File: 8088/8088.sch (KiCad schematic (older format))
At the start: 91 parts, among them CON1 BARREL_JACK, P1 CONN_02X20, P2 CONN_01X02, SW1 STEP_CLK, SW2 RESET, SW3 PWR, U1 8284, U10 2114, U11 ULN2803ADWR, U12 74LS14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

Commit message: Fixed schematic errors and added custom component footprints for the switches/PBs
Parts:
- added D31: AD0, LEDs:LED_1206_HandSoldering, symbol Led_Small
- added D32: AD1, LEDs:LED_1206_HandSoldering, symbol Led_Small
- added D33: AD2, LEDs:LED_1206_HandSoldering, symbol Led_Small
- added D34: AD3, LEDs:LED_1206_HandSoldering, symbol Led_Small
- added D35: PWR, LEDs:LED_1206_HandSoldering, symbol Led_Small
- added R33, R34, R35, R36: 1K, Resistors_SMD:R_0805_HandSoldering, symbol R_Small
- added R37: 220, Resistors_SMD:R_0805_HandSoldering, symbol R_Small
- added unit 2 of U12
- added unit 3 of U12
- added unit 4 of U12
- added unit 5 of U12
- D27: value AD0 -> DEN
- D28: value AD2 -> IO/~M
- D29: value AD3 -> RD
- D30: value AD4 -> WR
- JP1: value PROG/READ -> CLK_SEL
- SW1, SW2: footprint (none) -> Library:PB2PIN
- SW3: footprint (none) -> Library:SPST-SLIDE
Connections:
- net labels added: IO/~M, ~DEN, ~RD, ~WR
- net labels removed: VDD
- wire segments 557 -> 536
- no-connect marks 26 -> 18
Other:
- moved on the sheet: D27, D28, D29, D30, R29, R30, R31, R32

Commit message: Started PCB
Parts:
- removed U16: LM7805, TO_SOT_Packages_SMD:TO-252-3_TabPin2, symbol LM7805
- added U16: 7805, TO_SOT_Packages_SMD:TO-252-3_TabPin2, symbol 7805
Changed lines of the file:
@@
-$EndComp
-$Comp
-L LM7805 U16
-U 1 1 59D01B37
-P 19300 7650
-F 0 "U16" H 19450 7454 50  0000 C CNN
-F 1 "LM7805" H 19300 7850 50  0000 C CNN
-F 2 "TO_SOT_Packages_SMD:TO-252-3_TabPin2" H 19300 7650 50  0001 C CNN
-F 3 "" H 19300 7650 50  0000 C CNN
-	1    19300 7650
-	1    0    0    -1
 $EndComp
 $Comp
@@
 	20550 8000 20550 7900
 Connection ~ 19900 8000
+$Comp
+L 7805 U16
+U 1 1 59C7D17F
+P 19300 7650
+F 0 "U16" H 19450 7454 50  0000 C CNN
+F 1 "7805" H 19300 7850 50  0000 C CNN
+F 2 "TO_SOT_Packages_SMD:TO-252-3_TabPin2" H 19300 7650 50  0001 C CNN
+F 3 "" H 19300 7650 50  0000 C CNN
+	1    19300 7650
+	1    0    0    -1
+$EndComp
 $EndSCHEMATC

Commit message: Initial PCB design finished
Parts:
- removed P1: CONN_02X20, Pin_Headers:Pin_Header_Straight_2x20_Pitch2.54mm, symbol CONN_02X20
- added P1: U3PA, Pin_Headers:Pin_Header_Straight_1x08_Pitch2.54mm, symbol CONN_01X08
- added P3: U3PB, Pin_Headers:Pin_Header_Straight_1x08_Pitch2.54mm, symbol CONN_01X08
- added P4: RX/TX, Pin_Headers:Pin_Header_Straight_1x02_Pitch2.54mm, symbol CONN_01X02
- added P5: U4PC, Pin_Headers:Pin_Header_Straight_1x06_Pitch2.54mm, symbol CONN_01X06
- added P6: U4PA, Pin_Headers:Pin_Header_Straight_1x08_Pitch2.54mm, symbol CONN_01X08
- added P7: U4PB, Pin_Headers:Pin_Header_Straight_1x08_Pitch2.54mm, symbol CONN_01X08
- added P8: GND, Pin_Headers:Pin_Header_Straight_2x02_Pitch2.54mm, symbol CONN_01X04
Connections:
- wire segments 536 -> 535
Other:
- moved on the sheet: P2

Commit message: Fixed schematic error
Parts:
- U10, U9: symbol 2114 -> 2114-RESCUE-8088
- U16: symbol 7805 -> 7805-RESCUE-8088
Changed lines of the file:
@@
 EESchema Schematic File Version 2
+LIBS:8088-rescue
 LIBS:8088
-LIBS:ab2_7segment
-LIBS:ab2_audio
-LIBS:ab2_buffer
-LIBS:ab2_capacitor
-LIBS:ab2_connectivity
-LIBS:ab2_dac
-LIBS:ab2_diode
-LIBS:ab2_gpio_expansion
-LIBS:ab2_header
-LIBS:ab2_idc
-LIBS:ab2_inductor
-LIBS:ab2_input_devices
-LIBS:ab2_jumper
-LIBS:ab2_lcd
-LIBS:ab2_led
-LIBS:ab2_memory
-LIBS:ab2_opamp
-LIBS:ab2_pot
-LIBS:ab2_power
-LIBS:ab2_regulator
-LIBS:ab2_relay
-LIBS:ab2_resistor
-LIBS:ab2_sensor
-LIBS:ab2_stepper
-LIBS:ab2_supply
-LIBS:ab2_terminal_block
-LIBS:ab2_test
-LIBS:ab2_transistor
-LIBS:ab2_uC
-LIBS:ab2_usb
-LIBS:ab2_xtal
 LIBS:74xx
 LIBS:adc-dac
@@
 $EndComp
 $Comp
-L 2114 U9
+L 2114-RESCUE-8088 U9
 U 1 1 59C4625B
 P 10150 11550
@@
 $EndComp
 $Comp
-L 2114 U10
+L 2114-RESCUE-8088 U10
 U 1 1 59C462B2
 P 12400 11550
@@
 $EndComp
 $Comp
-L 7805 U16
+L 7805-RESCUE-8088 U16
 U 1 1 59C7D17F
 P 19300 7650

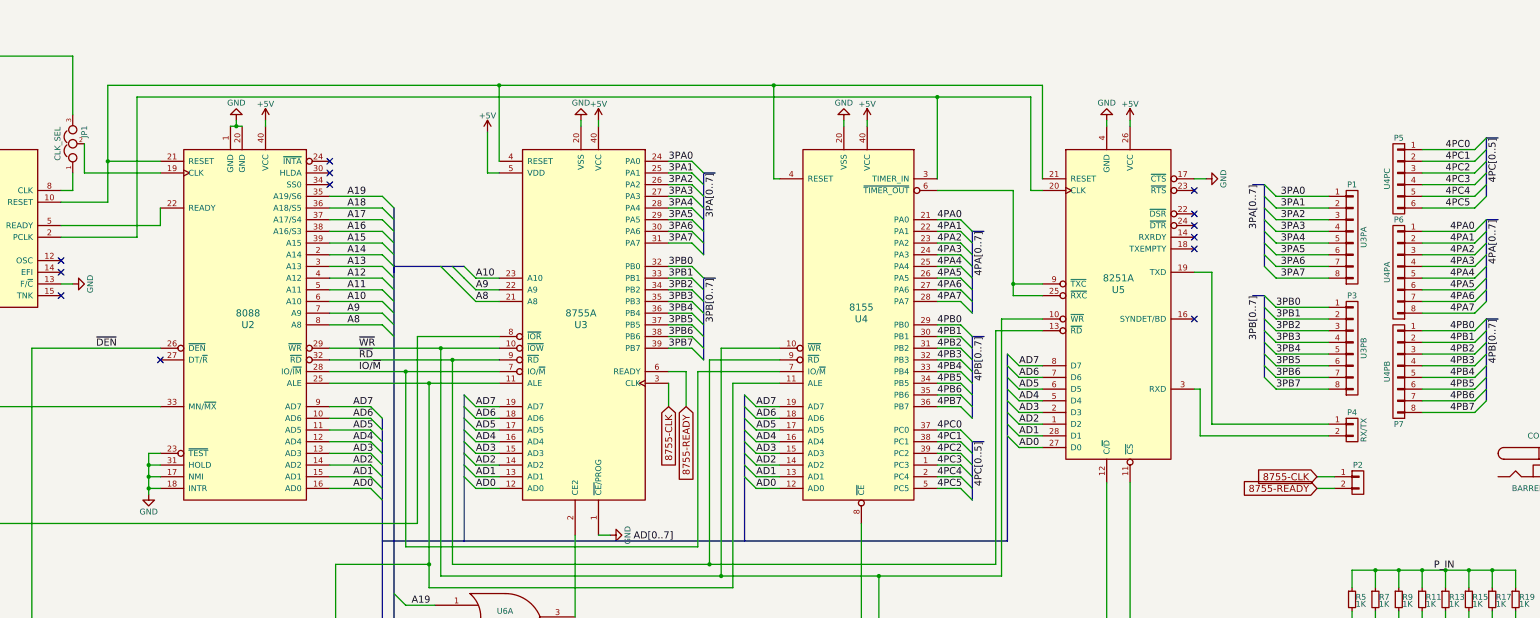
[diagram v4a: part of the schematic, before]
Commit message: Adding IO headers to schematic
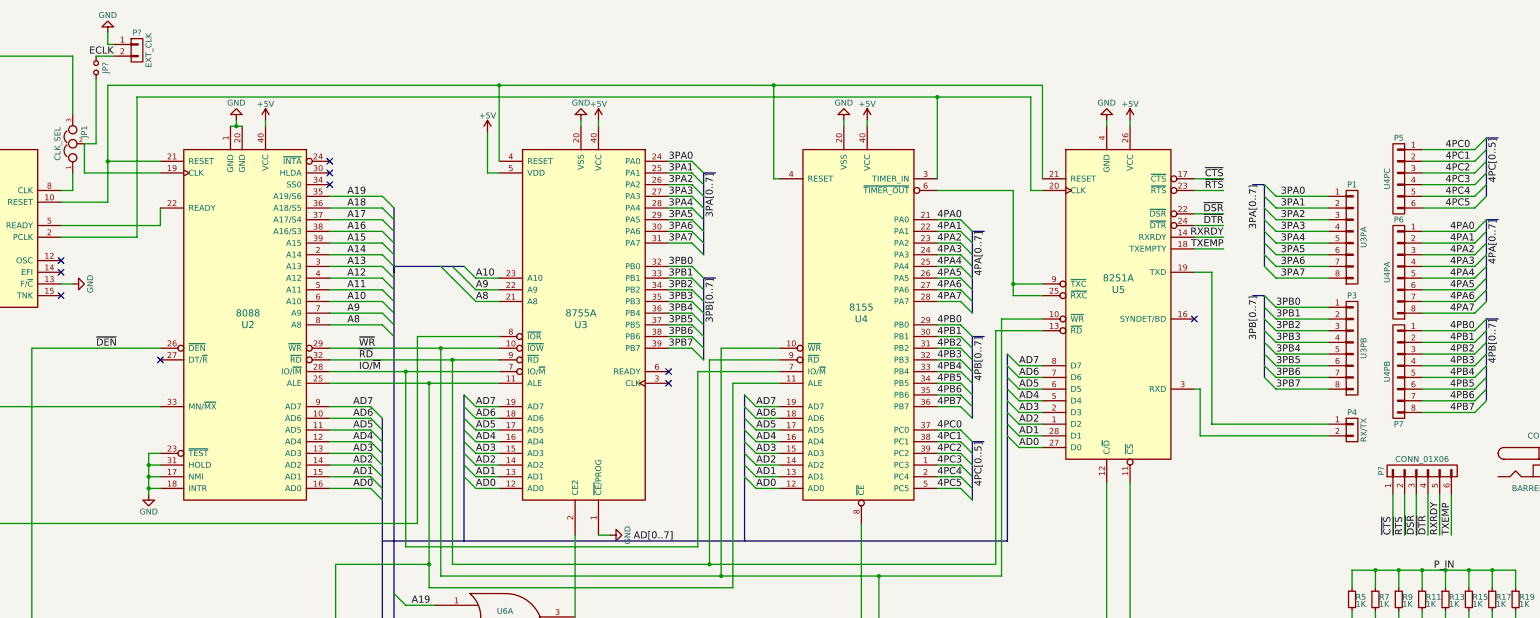
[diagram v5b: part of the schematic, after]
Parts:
- removed P2: CONN_01X02, Pin_Headers:Pin_Header_Straight_1x02_Pitch2.54mm, symbol CONN_01X02
- added JP?: Jumper_NO_Small, symbol Jumper_NO_Small
- added P?: EXT_CLK, symbol CONN_01X02
- added P?: CONN_01X06, symbol CONN_01X06
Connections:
- net GND: now also P?.1 (P1); no longer U5.17 (~CTS)
- net RXRDY: now reaches U5.14 (RXRDY)
- net RXRDY: now also P?.5 (P5)
- net TXEMP: now reaches U5.18 (TXEMPTY)
- net TXEMP: now also P?.6 (P6)
- net ~DSR: now reaches U5.22 (~DSR)
- net ~DSR: now also P?.3 (P3)
- net ~RTS: now reaches U5.23 (~RTS)
- net ~RTS: now also P?.2 (P2)
- net ~DTR: now reaches U5.24 (~DTR)
- net ~DTR: now also P?.4 (P4)
- net at JP1.2, U2.19 (CLK): now also JP?.2
- net 8755-CLK: no longer names the net of U3.3 (CLK)
- net 8755-READY: no longer names the net of U3.6 (READY)
- new net ECLK: JP?.1, P?.2 (P2)
- new net ~CTS: P?.1 (P1), U5.17 (~CTS)
- no-connect marks 18 -> 15
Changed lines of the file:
@@
 EESchema Schematic File Version 2
-LIBS:8088-rescue
 LIBS:8088
+LIBS:ab2_7segment
+LIBS:ab2_audio
+LIBS:ab2_buffer
+LIBS:ab2_capacitor
+LIBS:ab2_connectivity
+LIBS:ab2_dac
+LIBS:ab2_diode
+LIBS:ab2_gpio_expansion
+LIBS:ab2_header
+LIBS:ab2_idc
+LIBS:ab2_inductor
+LIBS:ab2_input_devices
+LIBS:ab2_jumper
+LIBS:ab2_lcd
+LIBS:ab2_led
+LIBS:ab2_memory
+LIBS:ab2_opamp
+LIBS:ab2_pot
+LIBS:ab2_power
+LIBS:ab2_regulator
+LIBS:ab2_relay
+LIBS:ab2_resistor
+LIBS:ab2_sensor
+LIBS:ab2_stepper
+LIBS:ab2_supply
+LIBS:ab2_terminal_block
+LIBS:ab2_test
+LIBS:ab2_transistor
+LIBS:ab2_uC
+LIBS:ab2_usb
+LIBS:ab2_xtal
 LIBS:74xx
 LIBS:adc-dac
@@
 $EndComp
 $Comp
-L 8251A U5
-U 1 1 59C452F9
-P 12350 6150
-F 0 "U5" H 13200 6100 60  0000 C CNN
-F 1 "8251A" H 13200 6200 60  0000 C CNN
-F 2 "Housings_DIP:DIP-28_W15.24mm_Socket" H 11850 5750 60  0001 C CNN
-F 3 "" H 11850 5750 60  0001 C CNN
-	1    12350 6150
-	1    0    0    -1
-$EndComp
-$Comp
 L 74LS138 U7
 U 1 1 59C45F6B
@@
 NoConn ~ 13850 6450
 $Comp
-L GND #PWR01
-U 1 1 59C4B0EE
-P 13950 5250
-F 0 "#PWR01" H 13950 5000 50  0001 C CNN
-F 1 "GND" H 13950 5100 50  0000 C CNN
-F 2 "" H 13950 5250 50  0000 C CNN
-F 3 "" H 13950 5250 50  0000 C CNN
-	1    13950 5250
-	0    -1   -1   0
-$EndComp
-NoConn ~ 13850 5350
-NoConn ~ 13850 5650
-NoConn ~ 13850 5750
-NoConn ~ 13850 5850
-NoConn ~ 13850 5550
-$Comp
 L Crystal Y1
 U 1 1 59C4CC7C
@@
 	1    0    0    -1
 $EndComp
-$Comp
-L CONN_01X02 P2
-U 1 1 59C994D5
-P 15250 7850
-F 0 "P2" H 15250 8000 50  0000 C CNN
-F 1 "CONN_01X02" V 15350 7850 50  0001 C CNN
-F 2 "Pin_Headers:Pin_Header_Straight_1x02_Pitch2.54mm" H 15250 7850 50  0001 C CNN
-F 3 "" H 15250 7850 50  0000 C CNN
-	1    15250 7850
-	1    0    0    -1
-$EndComp
-Text GLabel 9350 7200 3    60   Input ~ 0
-8755-CLK
-Text GLabel 9500 7200 3    60   Input ~ 0
-8755-READY
-Text GLabel 14900 7900 0    60   Input ~ 0
-8755-READY
-Text GLabel 14900 7800 0    60   Input ~ 0
-8755-CLK
 Entry Wire Line
 	9550 6000 9650 6100
@@
 Wire Wire Line
 	14000 6050 14000 7350
-Wire Wire Line
-	15050 7800 14900 7800
-Wire Wire Line
-	15050 7900 14900 7900
-Wire Wire Line
-	9350 6900 9500 6900
-Wire Wire Line
-	9500 6900 9500 7200
-Wire Wire Line
-	9350 7000 9350 7200
 Wire Bus Line
 	9650 6100 9650 6800
@@
 	9350 5100 9550 5100
 Wire Wire Line
-	13950 5250 13850 5250
+	13850 5250 14100 5250
 Wire Bus Line
 	11950 5700 11950 6400
@@
 Text Label 16000 5500 0    60   ~ 0
 4PC5
+$Comp
+L 8251A U5
+U 1 1 59C452F9
+P 12350 6150
+F 0 "U5" H 13200 6100 60  0000 C CNN
+F 1 "8251A" H 13200 6200 60  0000 C CNN
+F 2 "Housings_DIP:DIP-28_W15.24mm_Socket" H 11850 5750 60  0001 C CNN
+F 3 "" H 11850 5750 60  0001 C CNN
+	1    12350 6150
+	1    0    0    -1
+$EndComp
+Wire Wire Line
+	13850 5350 14100 5350
+Wire Wire Line
+	13850 5550 14100 5550
+Wire Wire Line
+	13850 5650 14100 5650
+Wire Wire Line
+	13850 5750 14100 5750
+Wire Wire Line
+	13850 5850 14100 5850
+$Comp
+L CONN_01X02 P?
+U 1 1 59D169E6
+P 4800 4150
+F 0 "P?" H 4800 4300 50  0000 C CNN
+F 1 "EXT_CLK" V 4900 4150 50  0000 C CNN
+F 2 "" H 4800 4150 50  0000 C CNN
+F 3 "" H 4800 4150 50  0000 C CNN
+	1    4800 4150
+	1    0    0    -1
+$EndComp
+$Comp
+L Jumper_NO_Small JP?
+U 1 1 59D16C96
+P 4450 4300
+F 0 "JP?" H 4450 4380 50  0000 C CNN
+F 1 "Jumper_NO_Small" H 4460 4240 50  0001 C CNN
+F 2 "" H 4450 4300 50  0000 C CNN
+F 3 "" H 4450 4300 50  0000 C CNN
+	1    4450 4300
+	0    1    1    0
+$EndComp
+Wire Wire Line
+	4600 4200 4450 4200
+Wire Wire Line
+	4450 4400 4450 4950
+Wire Wire Line
+	4450 4950 4350 4950
+$Comp
+L GND #PWR?
+U 1 1 59D18875
+P 4550 4000
+F 0 "#PWR?" H 4550 3750 50  0001 C CNN
+F 1 "GND" H 4550 3850 50  0000 C CNN
+F 2 "" H 4550 4000 50  0000 C CNN
+F 3 "" H 4550 4000 50  0000 C CNN
+	1    4550 4000
+	-1   0    0    1
+$EndComp
+Text Label 4600 4200 2    60   ~ 0
+ECLK
+Wire Wire Line
+	4600 4100 4550 4100
+Wire Wire Line
+	4550 4100 4550 4000
+Text Label 14100 5250 2    60   ~ 0
+~CTS
+Text Label 14100 5350 2    60   ~ 0
+~RTS
+Text Label 14100 5550 2    60   ~ 0
+~DSR
+Text Label 14100 5650 2    60   ~ 0
+~DTR
+Text Label 14100 5750 2    60   ~ 0
+RXRDY
+Text Label 14100 5850 2    60   ~ 0
+TXEMP
+NoConn ~ 9350 6900
+NoConn ~ 9350 7000
+$Comp
+L CONN_01X06 P?
+U 1 1 59D32665
+P 15800 7750
+F 0 "P?" H 15800 8100 50  0000 C CNN
+F 1 "CONN_01X06" V 15900 7750 50  0000 C CNN
+F 2 "" H 15800 7750 50  0000 C CNN
+F 3 "" H 15800 7750 50  0000 C CNN
+	1    15800 7750
+	0    -1   -1   0
+$EndComp
+Wire Wire Line
+	15550 7950 15550 8300
+Wire Wire Line
+	15650 7950 15650 8300
+Wire Wire Line
+	15750 7950 15750 8300
+Wire Wire Line
+	15850 7950 15850 8300
+Wire Wire Line
+	15950 7950 15950 8300
+Wire Wire Line
+	16050 7950 16050 8300
+Text Label 15550 8300 1    60   ~ 0
+~CTS
+Text Label 15650 8300 1    60   ~ 0
+~RTS
+Text Label 15750 8300 1    60   ~ 0
+~DSR
+Text Label 15850 8300 1    60   ~ 0
+~DTR
+Text Label 15950 8300 1    60   ~ 0
+RXRDY
+Text Label 16050 8300 1    60   ~ 0
+TXEMP
 $EndSCHEMATC

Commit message: Updated libraries. Added IO headers to schematics. TODO: Route ISA bus
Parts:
- added BUS?: BUSPC, symbol BUSPC
- added P?: CONN_01X15, symbol CONN_01X15
- added P? (x2): CONN_01X05, symbol CONN_01X05
- added P? (x2): CONN_01X08, symbol CONN_01X08
- added U?: MAX232, symbol MAX232
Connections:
- net A0: now also P?.1 (P1)
- net A1: now also P?.2 (P2)
- net A10: now also P?.11 (P11)
- net A11: now also P?.12 (P12)
- net A12: now also P?.13 (P13)
- net A13: now also P?.14 (P14)
- net A14: now also P?.15 (P15)
- net A15: now also P?.1 (P1)
- net A16: now also P?.2 (P2)
- net A17: now also P?.3 (P3)
- net A18: now also P?.4 (P4)
- net A19: now also P?.5 (P5)
- net A2: now also P?.3 (P3)
- net A3: now also P?.4 (P4)
- net A4: now also P?.5 (P5)
- net A5: now also P?.6 (P6)
- net A6: now also P?.7 (P7)
- net A7: now also P?.8 (P8)
- net A8: now also P?.9 (P9)
- net A9: now also P?.10 (P10)
- net AD0: now also P?.1 (P1)
- net AD1: now also P?.2 (P2)
- net AD2: now also P?.3 (P3)
- net AD3: now also P?.4 (P4)
- net AD4: now also P?.5 (P5)
- net AD5: now also P?.6 (P6)
- net AD6: now also P?.7 (P7)
- net AD7: now also P?.8 (P8)
- net IO/~M: now also P?.1 (P1)
- net ~RD: now also P?.3 (P3)
- net ~WR: now also P?.4 (P4)
- net ALE: now reaches U2.25 (ALE), U3.11 (ALE), U4.11 (ALE), U8.11 (STB)
- net ALE: now also P?.5 (P5)
- net ~IOR: now reaches R4.1, U1.7 (~AEN2), U2.33 (MN/~MX), U3.8 (~IOR), U7.6 (E3)
- net ~IOR: now also P?.2 (P2)
- net DEC6: now reaches U4.8 (~CE), U7.9 (O6)
- net DEC6: now also P?.7 (P7)
- net DEC7: now reaches U5.11 (~CS), U7.7 (O7)
- net DEC7: now also P?.8 (P8)
- net DEC5: now reaches U12.1, U7.10 (O5)
- net DEC5: now also P?.6 (P6)
- net DEC4: now reaches U7.11 (O4)
- net DEC4: now also P?.5 (P5)
- net DEC3: now reaches U7.12 (O3)
- net DEC3: now also P?.4 (P4)
- net DEC2: now reaches U7.13 (O2)
- net DEC2: now also P?.3 (P3)
- net DEC1: now reaches U7.14 (O1)
- net DEC1: now also P?.2 (P2)
- net DEC0: now reaches U6.5, U7.15 (O0)
- net DEC0: now also P?.1 (P1)
- no-connect marks 15 -> 11
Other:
- moved on the sheet: P8

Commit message: Second board revision down. Added bling :)
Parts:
- removed BUS?: BUSPC, symbol BUSPC
- removed JP?: Jumper_NO_Small, symbol Jumper_NO_Small
- removed P?: EXT_CLK, symbol CONN_01X02
- removed U?: MAX232, symbol MAX232
- added D36, D37: 1N914, Diodes_ThroughHole:D_DO-35_SOD27_P2.54mm_Vertical_AnodeUp, symbol D_Small
- added JP2: JUMPER3, Pin_Headers:Pin_Header_Straight_1x03_Pitch2.54mm, symbol JUMPER3
- P10: renamed from P?; footprint (none) -> Pin_Headers:Pin_Header_Straight_1x15_Pitch2.54mm
- P11, P12: renamed from P?; footprint (none) -> Pin_Headers:Pin_Header_Straight_1x05_Pitch2.54mm
- P13, P14: renamed from P?; footprint (none) -> Pin_Headers:Pin_Header_Straight_1x08_Pitch2.54mm
- P9: renamed from P?; footprint (none) -> Pin_Headers:Pin_Header_Straight_1x06_Pitch2.54mm
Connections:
- net +5V: now also D36.1 (K)
- net ECLK: now also D36.2 (A), D37.1 (K), JP2.2
- net GND: now also D37.2 (A)
- no-connect marks 11 -> 13

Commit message: Fixed chip socket widths
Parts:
- removed U10, U9: 2114, Housings_DIP:DIP-18_W7.62mm_Socket, symbol 2114-RESCUE-8088
- added U10, U9: 2114, Housings_DIP:DIP-18_W7.62mm, symbol 2114
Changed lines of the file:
@@
 $EndComp
 $Comp
-L 2114-RESCUE-8088 U9
-U 1 1 59C4625B
-P 10150 11550
-F 0 "U9" H 10100 11700 60  0000 C CNN
-F 1 "2114" H 10100 11800 60  0000 C CNN
-F 2 "Housings_DIP:DIP-18_W7.62mm_Socket" H 9250 10950 60  0001 C CNN
-F 3 "" H 9250 10950 60  0001 C CNN
-	1    10150 11550
-	1    0    0    -1
-$EndComp
-$Comp
-L 2114-RESCUE-8088 U10
-U 1 1 59C462B2
-P 12400 11550
-F 0 "U10" H 12350 11700 60  0000 C CNN
-F 1 "2114" H 12350 11800 60  0000 C CNN
-F 2 "Housings_DIP:DIP-18_W7.62mm_Socket" H 11500 10950 60  0001 C CNN
-F 3 "" H 11500 10950 60  0001 C CNN
-	1    12400 11550
-	1    0    0    -1
-$EndComp
-$Comp
 L 74LS32 U6
 U 1 1 59C46397
@@
 Text Label 5400 4000 2    60   ~ 0
 ECLK
+$Comp
+L 2114 U9
+U 1 1 59D1C1F6
+P 10150 11550
+F 0 "U9" H 10100 11700 60  0000 C CNN
+F 1 "2114" H 10100 11800 60  0000 C CNN
+F 2 "Housings_DIP:DIP-18_W7.62mm" H 9250 10950 60  0001 C CNN
+F 3 "" H 9250 10950 60  0001 C CNN
+	1    10150 11550
+	1    0    0    -1
+$EndComp
+$Comp
+L 2114 U10
+U 1 1 59D1C386
+P 12400 11550
+F 0 "U10" H 12350 11700 60  0000 C CNN
+F 1 "2114" H 12350 11800 60  0000 C CNN
+F 2 "Housings_DIP:DIP-18_W7.62mm" H 11500 10950 60  0001 C CNN
+F 3 "" H 11500 10950 60  0001 C CNN
+	1    12400 11550
+	1    0    0    -1
+$EndComp
 $EndSCHEMATC
